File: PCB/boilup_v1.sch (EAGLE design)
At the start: 30 parts, among them IC1 THS4211, J1 USB-MICROB, U1 STM32F0_LQFP64, U2 SPX3819-3.3

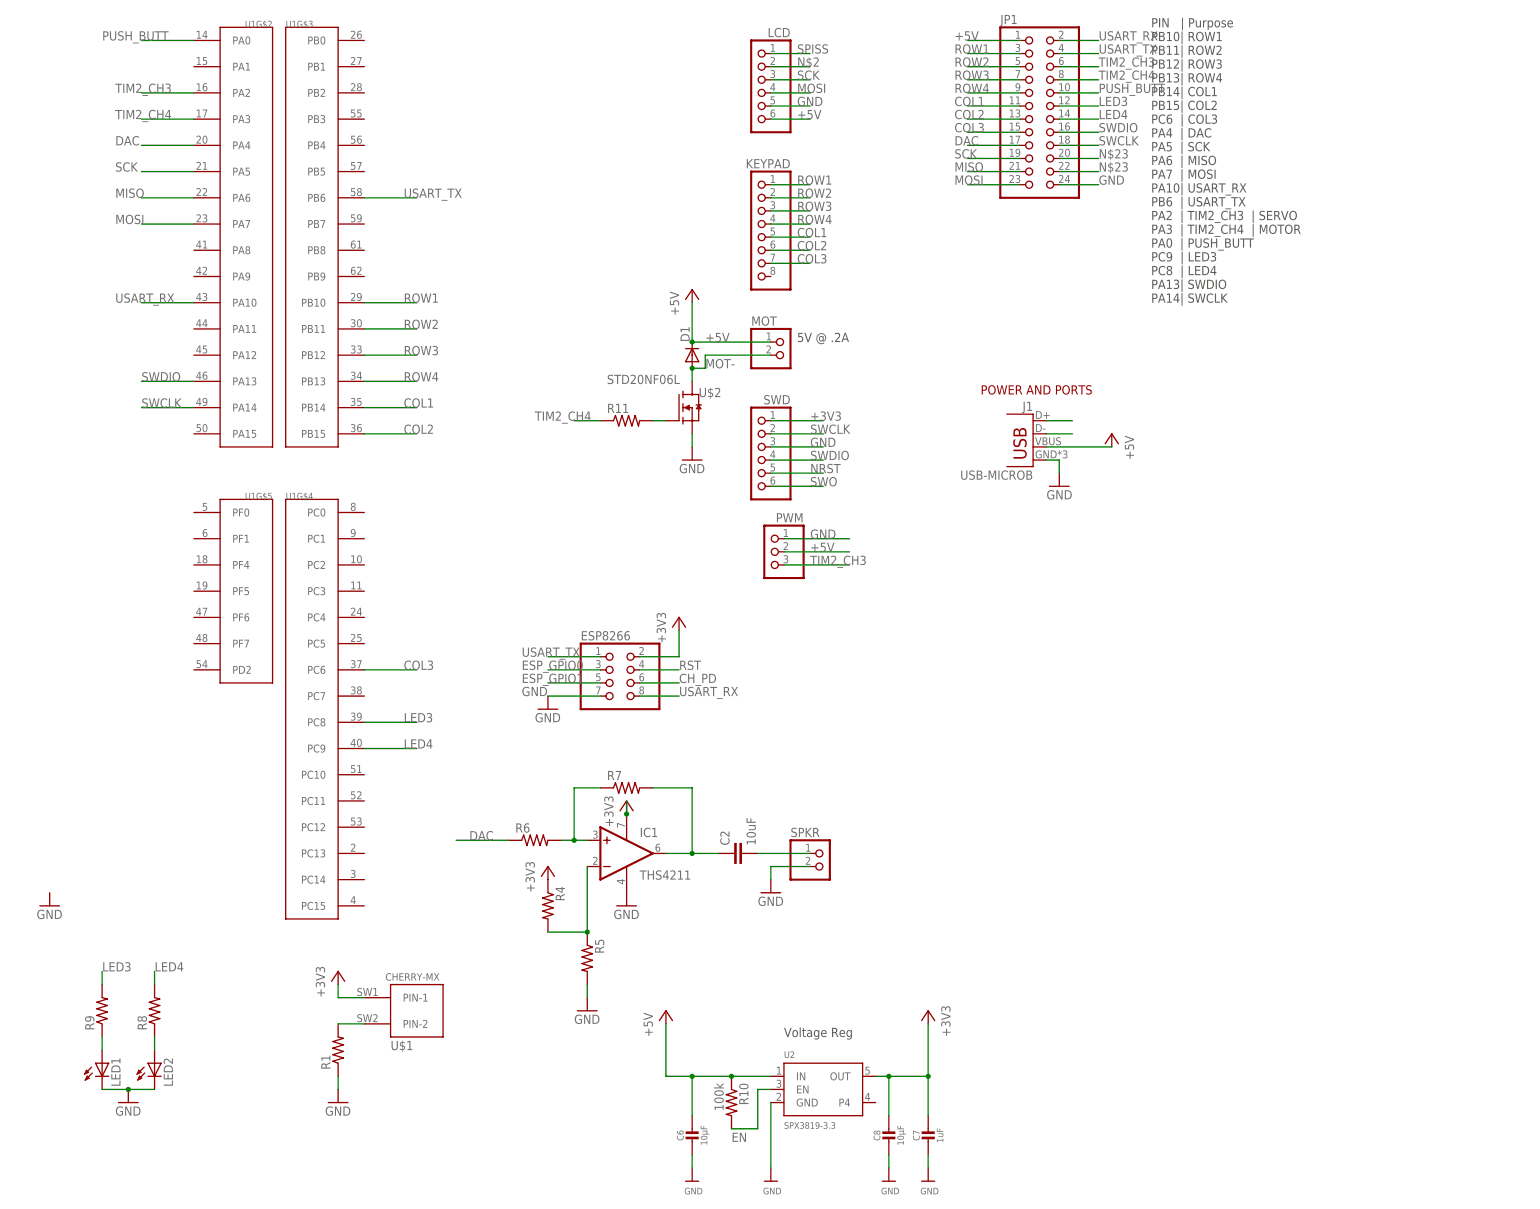
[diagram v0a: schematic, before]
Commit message: Initial routing + pinout
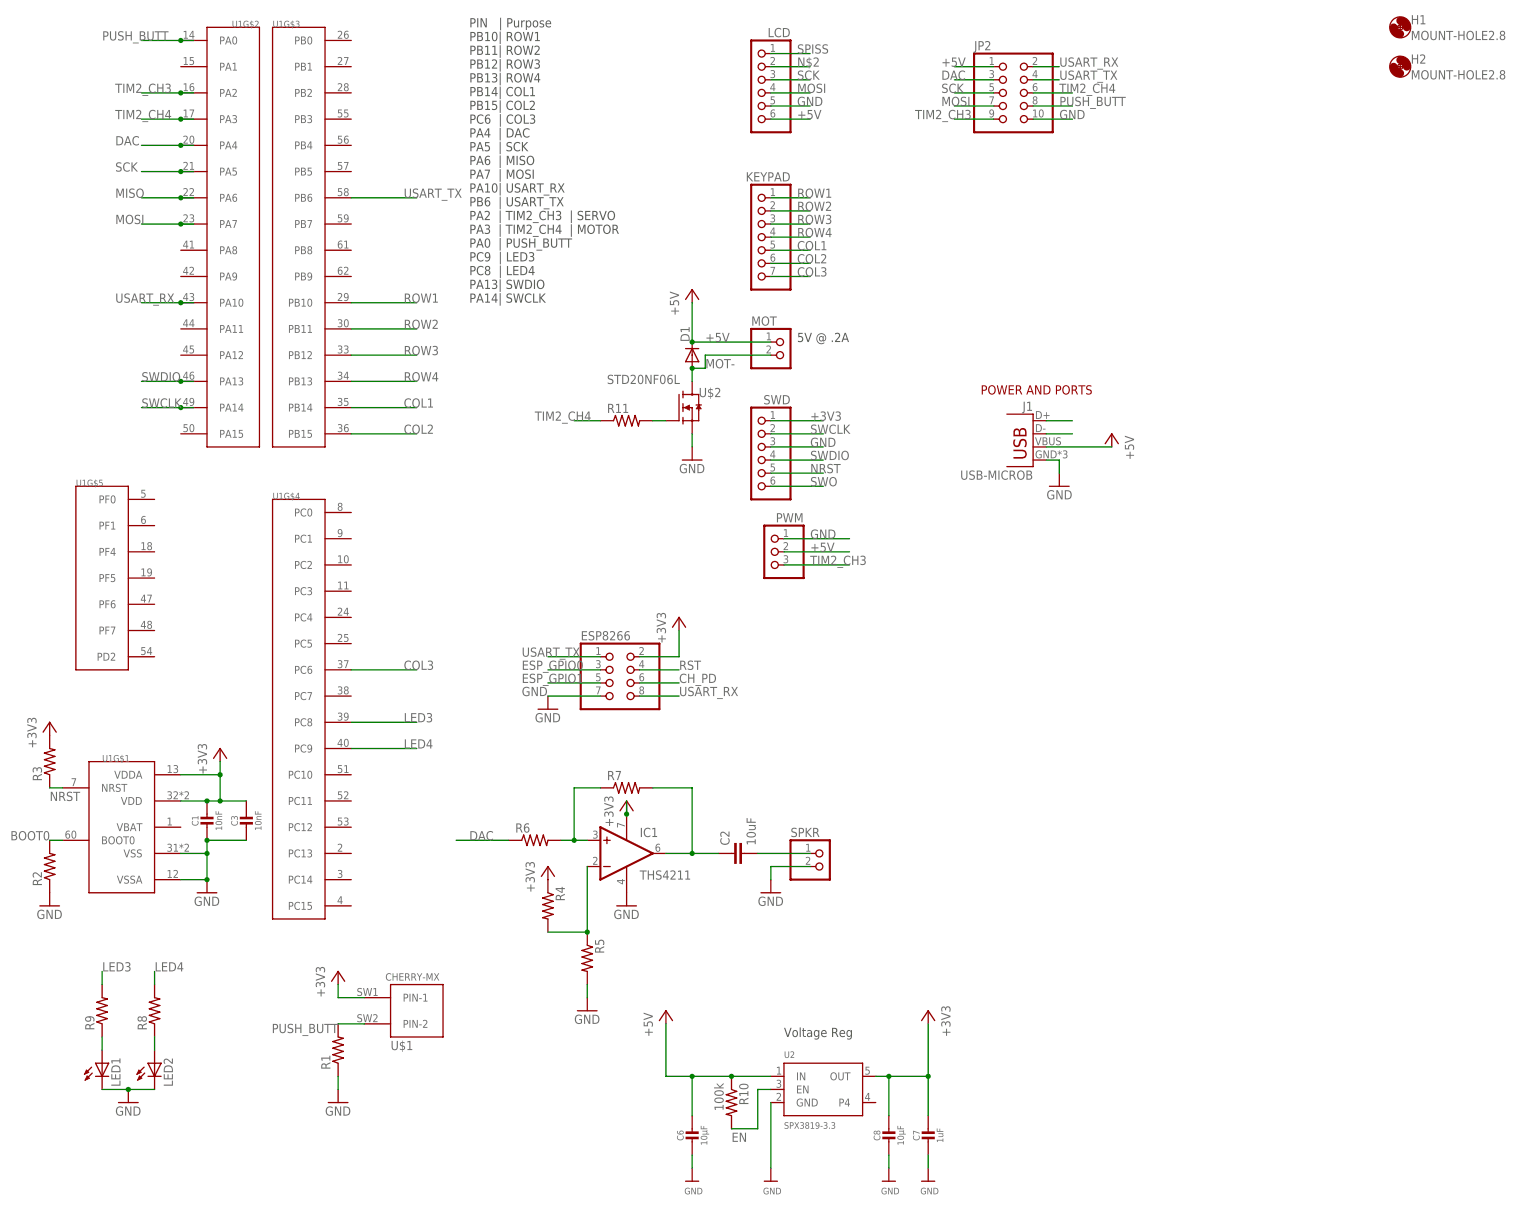
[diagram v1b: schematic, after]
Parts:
- removed JP1: (no value), pinhead:PINHD-2X12
- added C1, C3: 10nF, microbuilder:CAP_CERAMIC0805-NOOUTLINE
- added H1, H2: MOUNT-HOLE2.8, holes:MOUNT-HOLE2.8
- added JP2: (no value), pinhead:PINHD-2X5
- added R2, R3: (no value), resistor:R-US_R0603
- KEYPAD: device pinhead:PINHD-1X8 -> pinhead:PINHD-1X7
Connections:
- removed net KETTLESWITCH: R1.2, U$1.PIN-2
- removed net N$22: JP1.22
- removed net N$23: JP1.20
- new net BOOT0: R2.2, U1G$1.BOOT0
- net +3V3: now also C1.1, C3.1, R3.2, U1G$1.VDD, U1G$1.VDDA
- net +5V: now also JP2.1; no longer JP1.1
- net COL1: no longer JP1.11
- net COL2: no longer JP1.13
- net COL3: no longer JP1.15
- net DAC: now also JP2.3; no longer JP1.17
- net GND: now also C1.2, C3.2, JP2.10, R2.1, U1G$1.VSS, U1G$1.VSSA; no longer JP1.24
- net LED3: no longer JP1.12
- net LED4: no longer JP1.14
- net MISO: no longer JP1.21
- net MOSI: now also JP2.7; no longer JP1.23
- net NRST: now also R3.1, U1G$1.NRST
- net PUSH_BUTT: now also JP2.8, R1.2, U$1.PIN-2; no longer JP1.10
- net ROW1: no longer JP1.3
- net ROW2: no longer JP1.5
- net ROW3: no longer JP1.7
- net ROW4: no longer JP1.9
- net SCK: now also JP2.5; no longer JP1.19
- net SWCLK: no longer JP1.18
- net SWDIO: no longer JP1.16
- net TIM2_CH3: now also JP2.9; no longer JP1.6
- net TIM2_CH4: now also JP2.6; no longer JP1.8
- net USART_RX: now also JP2.2; no longer JP1.2
- net USART_TX: now also JP2.4; no longer JP1.4
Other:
- moved on the sheet: U1G$2, U1G$3, U1G$4, U1G$5
